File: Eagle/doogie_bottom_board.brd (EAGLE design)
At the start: 92.9 x 98 mm, 32 parts, among them Q1 TEFT4300, Q2 TEFT4300, Q3 TEFT4300, Q4 TEFT4300, Q6 IRF9530, T1 BC337, T2 BC337, T3 BC337

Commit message: Add H-bridge name on bottom board silk
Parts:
- U1: value (none) -> TB6612FNG; device pololu:TB6612FNG -> doogie:TB6612FNG
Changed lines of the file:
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@@
 <drawing>
 <settings>
-<setting alwaysvectorfont="yes"/>
+<setting alwaysvectorfont="no"/>
 <setting keepoldvectorfont="yes"/>
 <setting verticaltext="up"/>
@@
 <attribute name="VALUE" x="25.146" y="14.097" size="0.6096" layer="27" font="vector" ratio="20" rot="R90"/>
 </element>
-<element name="U1" library="pololu" package="TB6612FNG" value="" x="0" y="15.24" smashed="yes" rot="R90">
-<attribute name="NAME" x="-10.16" y="7.62" size="1.27" layer="25" font="vector" ratio="20" rot="R180" align="top-left"/>
+<element name="U1" library="doogie" package="TB6612FNG" value="TB6612FNG" x="0" y="15.24" smashed="yes" rot="R90">
+<attribute name="NAME" x="-10.287" y="7.62" size="1.27" layer="25" font="vector" ratio="20" rot="R180" align="top-left"/>
+<attribute name="VALUE" x="0" y="17.526" size="1.27" layer="25" font="vector" ratio="20" rot="R180" align="center"/>
 </element>
 <element name="S1" library="doogie" package="M9040P" package3d_urn="urn:adsk.eagle:package:27676/1" value="" x="42.164" y="-27.432" smashed="yes" rot="R180">

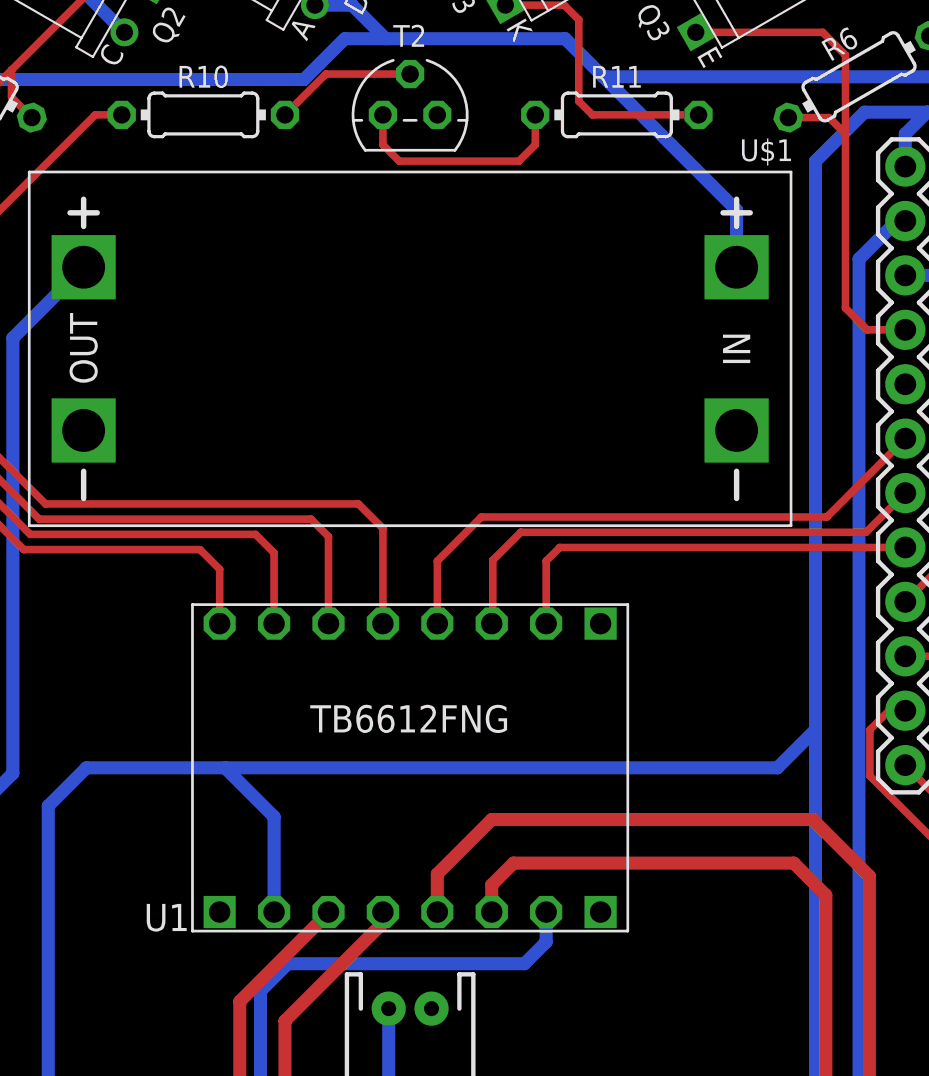
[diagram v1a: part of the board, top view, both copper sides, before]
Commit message: Add DC-DC name on silk
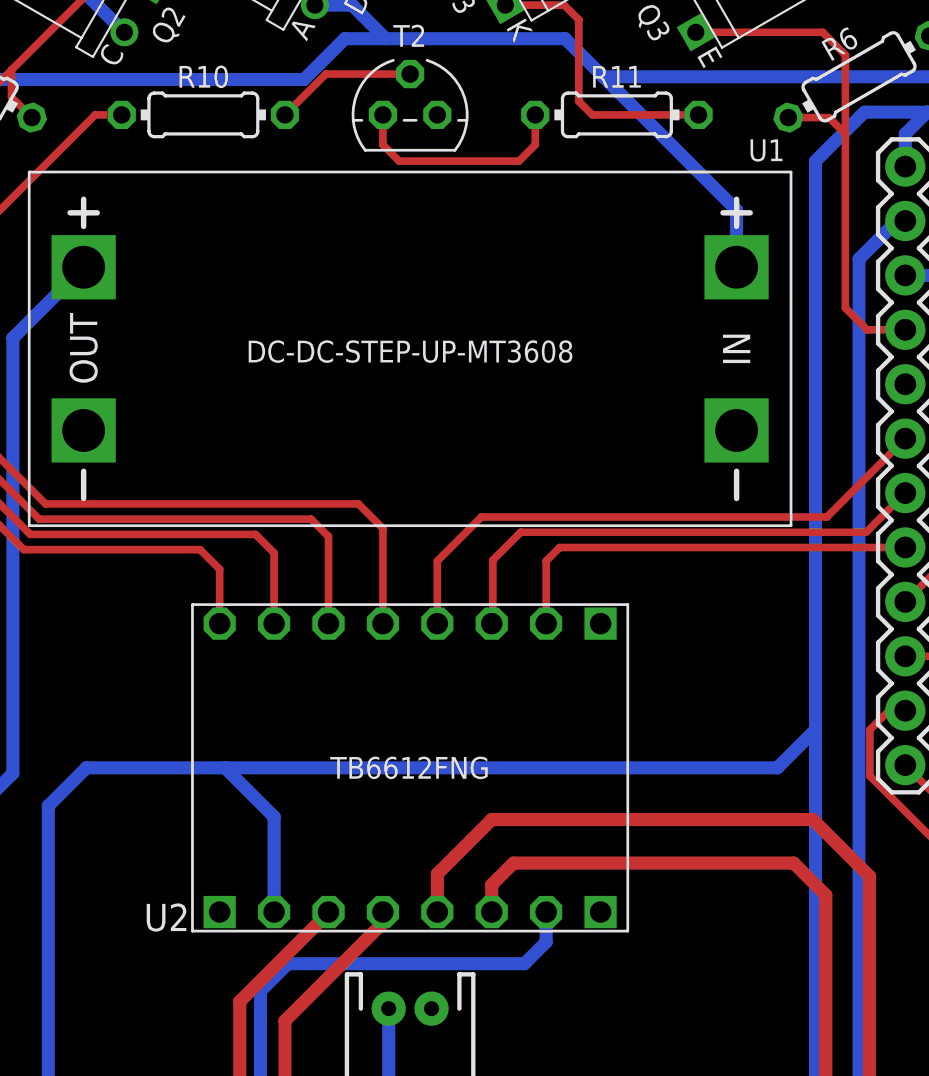
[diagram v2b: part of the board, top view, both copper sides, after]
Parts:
- removed U$1: DC-DC-STEP-UP-MT3608, diy-modules:DC-DC-STEP-UP-MT3608
- added U2: TB6612FNG, doogie:TB6612FNG
- U1: value TB6612FNG -> DC-DC-STEP-UP-MT3608; device doogie:TB6612FNG -> diy-modules:DC-DC-STEP-UP-MT3608
- moved U1 19.6 mm to (0.00, 34.8), turned to 0 degrees
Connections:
- net 3.3V: now also U2.2; no longer U1.2
- net 6V: now also U1.IN+, U2.7; no longer U$1.IN+, U1.7
- net FILLING_POLYGON: now also U1.IN-, U1.OUT-, U2.1, U2.16, U2.8; no longer U$1.IN-, U$1.OUT-, U1.1, U1.16, U1.8
- net H-BRIDGE_!STDBY: now also U2.12; no longer U1.12
- net MOTOR_LEFT_EN1: now also U2.11; no longer U1.11
- net MOTOR_LEFT_EN2: now also U2.10; no longer U1.10
- net MOTOR_LEFT_O1: now also U2.3; no longer U1.3
- net MOTOR_LEFT_O2: now also U2.4; no longer U1.4
- net MOTOR_LEFT_PWM: now also U2.9; no longer U1.9
- net MOTOR_RIGHT_EN1: now also U2.13; no longer U1.13
- net MOTOR_RIGHT_EN2: now also U2.14; no longer U1.14
- net MOTOR_RIGHT_O1: now also U2.6; no longer U1.6
- net MOTOR_RIGHT_O2: now also U2.5; no longer U1.5
- net MOTOR_RIGHT_PWM: now also U2.15; no longer U1.15
- net N$5: now also U1.OUT+; no longer U$1.OUT+
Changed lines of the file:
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@@
 <drawing>
 <settings>
-<setting alwaysvectorfont="no"/>
+<setting alwaysvectorfont="yes"/>
 <setting keepoldvectorfont="yes"/>
 <setting verticaltext="up"/>
@@
 <layer number="14" name="Route14" color="1" fill="6" visible="no" active="no"/>
 <layer number="15" name="Route15" color="4" fill="6" visible="no" active="no"/>
-<layer number="16" name="Bottom" color="1" fill="1" visible="yes" active="yes"/>
+<layer number="16" name="Bottom" color="1" fill="1" visible="no" active="yes"/>
 <layer number="17" name="Pads" color="2" fill="1" visible="yes" active="yes"/>
 <layer number="18" name="Vias" color="14" fill="1" visible="yes" active="yes"/>
@@
 <attribute name="VALUE" x="31.75" y="17.907" size="1.27" layer="27" rot="R180"/>
 </element>
-<element name="U$1" library="diy-modules" package="DC-DC-STEP-UP-MT3608" value="DC-DC-STEP-UP-MT3608" x="0" y="34.798" smashed="yes">
+<element name="U1" library="diy-modules" package="DC-DC-STEP-UP-MT3608" value="DC-DC-STEP-UP-MT3608" x="0" y="34.798" smashed="yes">
 <attribute name="NAME" x="16.637" y="43.561" size="1.016" layer="25" font="vector" ratio="20" align="bottom-center"/>
-<attribute name="VALUE" x="0" y="25.273" size="1.27" layer="27" align="top-center"/>
+<attribute name="VALUE" x="0" y="34.671" size="1.016" layer="25" font="vector" ratio="20" align="center"/>
 </element>
 <element name="T1" library="transistor" library_urn="urn:adsk.eagle:library:402" package="TO92" package3d_urn="urn:adsk.eagle:package:28523/2" value="BC337" x="-35.56" y="20.828" smashed="yes">
@@
 <attribute name="VALUE" x="25.146" y="14.097" size="0.6096" layer="27" font="vector" ratio="20" rot="R90"/>
 </element>
-<element name="U1" library="doogie" package="TB6612FNG" value="TB6612FNG" x="0" y="15.24" smashed="yes" rot="R90">
+<element name="U2" library="doogie" package="TB6612FNG" value="TB6612FNG" x="0" y="15.24" smashed="yes" rot="R90">
 <attribute name="NAME" x="-10.287" y="7.62" size="1.27" layer="25" font="vector" ratio="20" rot="R180" align="top-left"/>
-<attribute name="VALUE" x="0" y="17.526" size="1.27" layer="25" font="vector" ratio="20" rot="R180" align="center"/>
+<attribute name="VALUE" x="0" y="15.24" size="1.016" layer="25" font="vector" ratio="20" rot="R180" align="center"/>
 </element>
 <element name="S1" library="doogie" package="M9040P" package3d_urn="urn:adsk.eagle:package:27676/1" value="" x="42.164" y="-27.432" smashed="yes" rot="R180">
@@
 <signals>
 <signal name="FILLING_POLYGON">
-<contactref element="U$1" pad="IN-"/>
+<contactref element="U1" pad="IN-"/>
 <contactref element="J1" pad="2"/>
-<contactref element="U1" pad="1"/>
-<contactref element="U1" pad="8"/>
-<contactref element="U1" pad="16"/>
+<contactref element="U2" pad="1"/>
+<contactref element="U2" pad="8"/>
+<contactref element="U2" pad="16"/>
 <contactref element="T1" pad="1"/>
 <contactref element="T2" pad="1"/>
@@
 <contactref element="J3" pad="1"/>
 <contactref element="J4" pad="1"/>
-<contactref element="U$1" pad="OUT-"/>
+<contactref element="U1" pad="OUT-"/>
 <contactref element="Q6" pad="G"/>
 <contactref element="J5" pad="1"/>
@@
 </signal>
 <signal name="N$5">
-<contactref element="U$1" pad="OUT+"/>
+<contactref element="U1" pad="OUT+"/>
 <contactref element="S2" pad="3"/>
 <wire x1="-28.067" y1="5.461" x2="-28.067" y2="-19.558" width="0.6096" layer="16"/>
@@
 <contactref element="J4" pad="4"/>
 <contactref element="J2" pad="12"/>
-<contactref element="U1" pad="2"/>
+<contactref element="U2" pad="2"/>
 <contactref element="Q1" pad="C"/>
 <contactref element="Q4" pad="C"/>
@@
 <signal name="MOTOR_LEFT_O1">
 <contactref element="J3" pad="6"/>
-<contactref element="U1" pad="3"/>
+<contactref element="U2" pad="3"/>
 <wire x1="-3.81" y1="8.509" x2="-3.81" y2="8.477" width="0.6096" layer="1"/>
 <wire x1="-3.81" y1="8.477" x2="-7.9502" y2="4.3368" width="0.6096" layer="1"/>
@@
 <signal name="MOTOR_LEFT_O2">
 <contactref element="J3" pad="5"/>
-<contactref element="U1" pad="4"/>
+<contactref element="U2" pad="4"/>
 <wire x1="-1.27" y1="8.509" x2="-1.27" y2="8.001" width="0.6096" layer="1"/>
 <wire x1="-1.27" y1="8.001" x2="-5.842" y2="3.429" width="0.6096" layer="1"/>
@@
 <signal name="MOTOR_RIGHT_O2">
 <contactref element="J4" pad="5"/>
-<contactref element="U1" pad="5"/>
+<contactref element="U2" pad="5"/>
 <wire x1="1.27" y1="8.509" x2="1.27" y2="10.287" width="0.6096" layer="1"/>
 <wire x1="1.27" y1="10.287" x2="3.81" y2="12.827" width="0.6096" layer="1"/>
@@
 </signal>
 <signal name="MOTOR_LEFT_PWM">
-<contactref element="U1" pad="9"/>
+<contactref element="U2" pad="9"/>
 <contactref element="J1" pad="6"/>
 <wire x1="-18.02878125" y1="25.4254" x2="-9.8044" y2="25.4254" width="0.3556" layer="1"/>
@@
 </signal>
 <signal name="MOTOR_LEFT_EN2">
-<contactref element="U1" pad="10"/>
+<contactref element="U2" pad="10"/>
 <contactref element="J1" pad="7"/>
 <wire x1="-7.2136" y1="26.1366" x2="-6.35" y2="25.273" width="0.3556" layer="1"/>
@@
 </signal>
 <signal name="MOTOR_LEFT_EN1">
-<contactref element="U1" pad="11"/>
+<contactref element="U2" pad="11"/>
 <contactref element="J1" pad="8"/>
 <wire x1="-4.6228" y1="26.8478" x2="-3.81" y2="26.035" width="0.3556" layer="1"/>
@@
 </signal>
 <signal name="MOTOR_RIGHT_EN1">
-<contactref element="U1" pad="13"/>
+<contactref element="U2" pad="13"/>
 <contactref element="J2" pad="7"/>
 <wire x1="23.114" y1="30.607" x2="19.4564" y2="26.9494" width="0.3556" layer="1"/>
@@
 </signal>
 <signal name="MOTOR_RIGHT_EN2">
-<contactref element="U1" pad="14"/>
+<contactref element="U2" pad="14"/>
 <contactref element="J2" pad="6"/>
 <wire x1="23.114" y1="28.067" x2="21.2852" y2="26.2382" width="0.3556" layer="1"/>
@@
 </signal>
 <signal name="MOTOR_RIGHT_PWM">
-<contactref element="U1" pad="15"/>
+<contactref element="U2" pad="15"/>
 <contactref element="J2" pad="5"/>
 <wire x1="23.114" y1="25.527" x2="6.985" y2="25.527" width="0.3556" layer="1"/>
@@
 </signal>
 <signal name="H-BRIDGE_!STDBY">
-<contactref element="U1" pad="12"/>
+<contactref element="U2" pad="12"/>
 <contactref element="J1" pad="9"/>
 <wire x1="-2.413" y1="27.559" x2="-1.27" y2="26.416" width="0.3556" layer="1"/>
@@
 </signal>
 <signal name="MOTOR_RIGHT_O1">
-<contactref element="U1" pad="6"/>
+<contactref element="U2" pad="6"/>
 <contactref element="J4" pad="6"/>
 <wire x1="3.81" y1="8.509" x2="3.81" y2="9.779" width="0.6096" layer="1"/>
@@
 </signal>
 <signal name="6V">
-<contactref element="U$1" pad="IN+"/>
-<contactref element="U1" pad="7"/>
+<contactref element="U1" pad="IN+"/>
+<contactref element="U2" pad="7"/>
 <contactref element="J2" pad="10"/>
 <contactref element="D1" pad="A"/>
